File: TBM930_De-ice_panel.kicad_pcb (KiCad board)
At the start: 2 copper layers, 190.5 x 101.6 mm, 91 parts, among them J1 SW_AIRFRAME_DE_ICE, J10 AVR-ISP-6, J11 Screw_Terminal_01x02, J2 SW_ICE_LIGHT, J3 SW_PROP_DE_ICE, J4 SW_WIND_SHIELD, J5 SW_PITOT_L_HTR, J6 SW_PITOT_R_HTR, J7 SW_INERT_SEP, J8 Barrel_Jack, J9 USB_B_Mini, SW1 SW_Push, SW2 SW_Push, U1 TLC5917IN, U2 TLC5917IN, U3 ATmega32U4-MU, Y1 Crystal_GND24

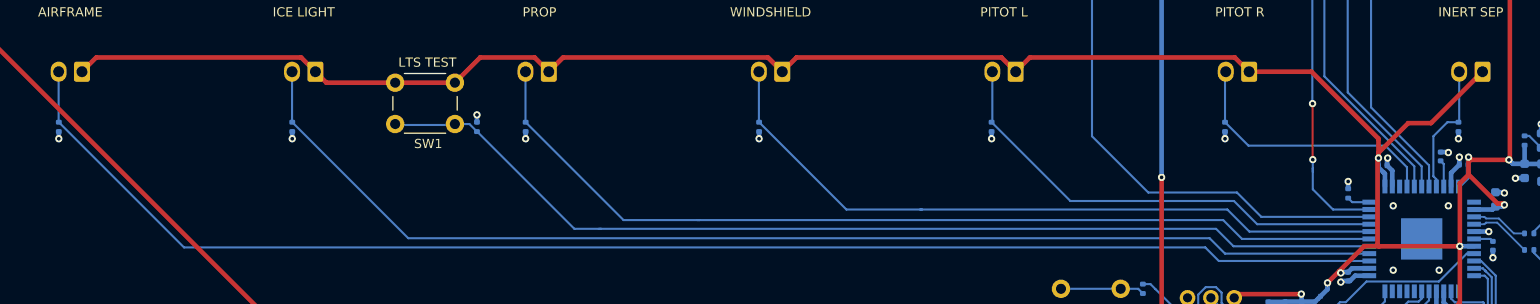
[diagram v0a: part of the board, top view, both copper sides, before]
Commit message: Fix switches back to ground connection (#4)
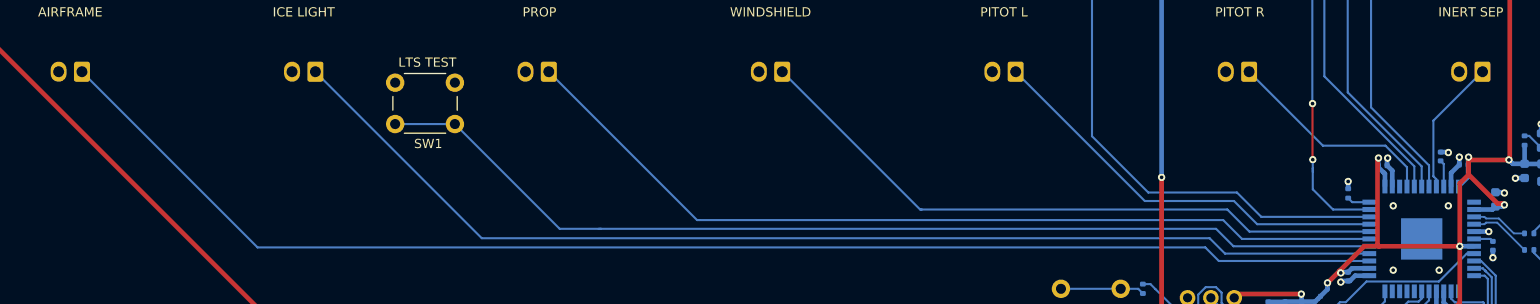
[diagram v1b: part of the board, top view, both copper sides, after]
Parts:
- removed R1, R12, R13, R14, R15, R16, R17, R18: 10k, Resistor_SMD:R_0402_1005Metric
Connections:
- J1 pad 1: +5V -> SW_AIRFRAME
- J1 pad 2: SW_AIRFRAME -> GND
- J2 pad 1: +5V -> SW_ICE_LIGHT
- J2 pad 2: SW_ICE_LIGHT -> GND
- J3 pad 1: +5V -> SW_PROP
- J3 pad 2: SW_PROP -> GND
- J4 pad 1: +5V -> SW_WINDSHIELD
- J4 pad 2: SW_WINDSHIELD -> GND
- J5 pad 1: +5V -> SW_PITOT_L
- J5 pad 2: SW_PITOT_L -> GND
- J6 pad 1: +5V -> SW_PITOT_R
- J6 pad 2: SW_PITOT_R -> GND
- J7 pad 1: +5V -> SW_INERT_SEP
- J7 pad 2: SW_INERT_SEP -> GND
- SW1 pad 1: +5V -> GND
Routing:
- net +5V: track 485.7 -> 316.5 mm
- net GND: track 38.0 -> 31.8 mm, vias 31 -> 23
- net SW_PROP: track 102.9 -> 96.8 mm
- net SW_WINDSHIELD: track 77.0 -> 71.1 mm
- net SW_PITOT_R: track 29.5 -> 23.6 mm
- net SW_PITOT_L: track 51.2 -> 45.4 mm
- net SW_ICE_LIGHT: track 128.6 -> 122.9 mm
- net SW_AIRFRAME: track 154.4 -> 148.6 mm

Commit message: Update schematic and PCB to use date
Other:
- board text added: "TBM 930 de-ice panel %%version%% %%date Designed by: Neil Enns"
- board text removed: "TBM 930 de-ice panel %%version%% Designed by: Neil Enns"

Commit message: Fix date placeholder on PCB
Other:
- board text added: "TBM 930 de-ice panel %%version%% %%date%% Designed by: Neil Enns"
- board text removed: "TBM 930 de-ice panel %%version%% %%date Designed by: Neil Enns"
